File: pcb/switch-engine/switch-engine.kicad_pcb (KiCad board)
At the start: 10 copper layers, 135 x 111 mm, 369 parts, among them J1 CONN_PCIE_PWR_8PIN, J10 CORTEX_DEBUG_ETM, J11 SMPM, J12 CONN_01X03, J13 PMOD_HOST, J14 ARF6-08-S-D-A-K-TR, J15 ARF6-08-S-D-A-K-TR, J16 CONN_01X10, J17 ARF6-08-S-D-A-K-TR, J18 ARF6-08-S-D-A-K-TR, J19 CONN_01X10, J2 CONN_IBC_MGMT, J20 0826-1G1T-23-F, J21 ARF6-08-S-D-A-K-TR, J22 ARF6-08-S-D-A-K-TR, J23 CONN_01X10, J24 SMPM, J26 RJ45, J3 CONN_01X03, J4 CORTEX_DEBUG_ETM, J5 FAN_01, J6 FAN_01, J7 JUMPER_0402, J8 XILINX_JTAG, J9 PMOD_HOST, M1 SCREWHOLE, M2 SCREWHOLE, M3 SCREWHOLE, M4 SCREWHOLE, M5 LOGO, M6 LOGO, M7 LOGO, M8 960-27-23-D-AB-0, M9 FAN, Q2 SSM6N58NU, SW1 SWITCH, SW2 SWITCH, U1 STM32L431-QFN48, U10 74LVC1T45, U11 74LVC1T45, U12 74LVC1T45, U13 MT25QU256ABA8E12-0AUT, U14 ECS-1612MV-250-CN, U15 SIT9121AI-2BF-XXS156.250000G, U17 AT24MAC402, U18 74LVC1T45, U19 74LVC1T45, U2 MYMGK1R812ERSR, U20 74LVC1T45, U21 74LVC1T45, U22 ECS-1612MV-250-CN, U23 KSZ9031RN, U24 ESD224DQAR, U25 SIT9121AI-2BF-XXS156.250000G, U26 ESD224DQAR, U27 SIT9121AI-2BF-XXS156.250000G, U28 ADP1740ACPZ-2.5-R7, U29 ADM3101E_QFN, U3 MYMGK1R812ERSR, U4 MYMGK00506ERSR, U5 MYMGK00504ERSR, U6 MYMGK00504ERSR, U7 ADP1740ACPZ-1.8-R7, U8 XCKU5P-2FFVB676I, U9 STM32H735-UFBGA176-25

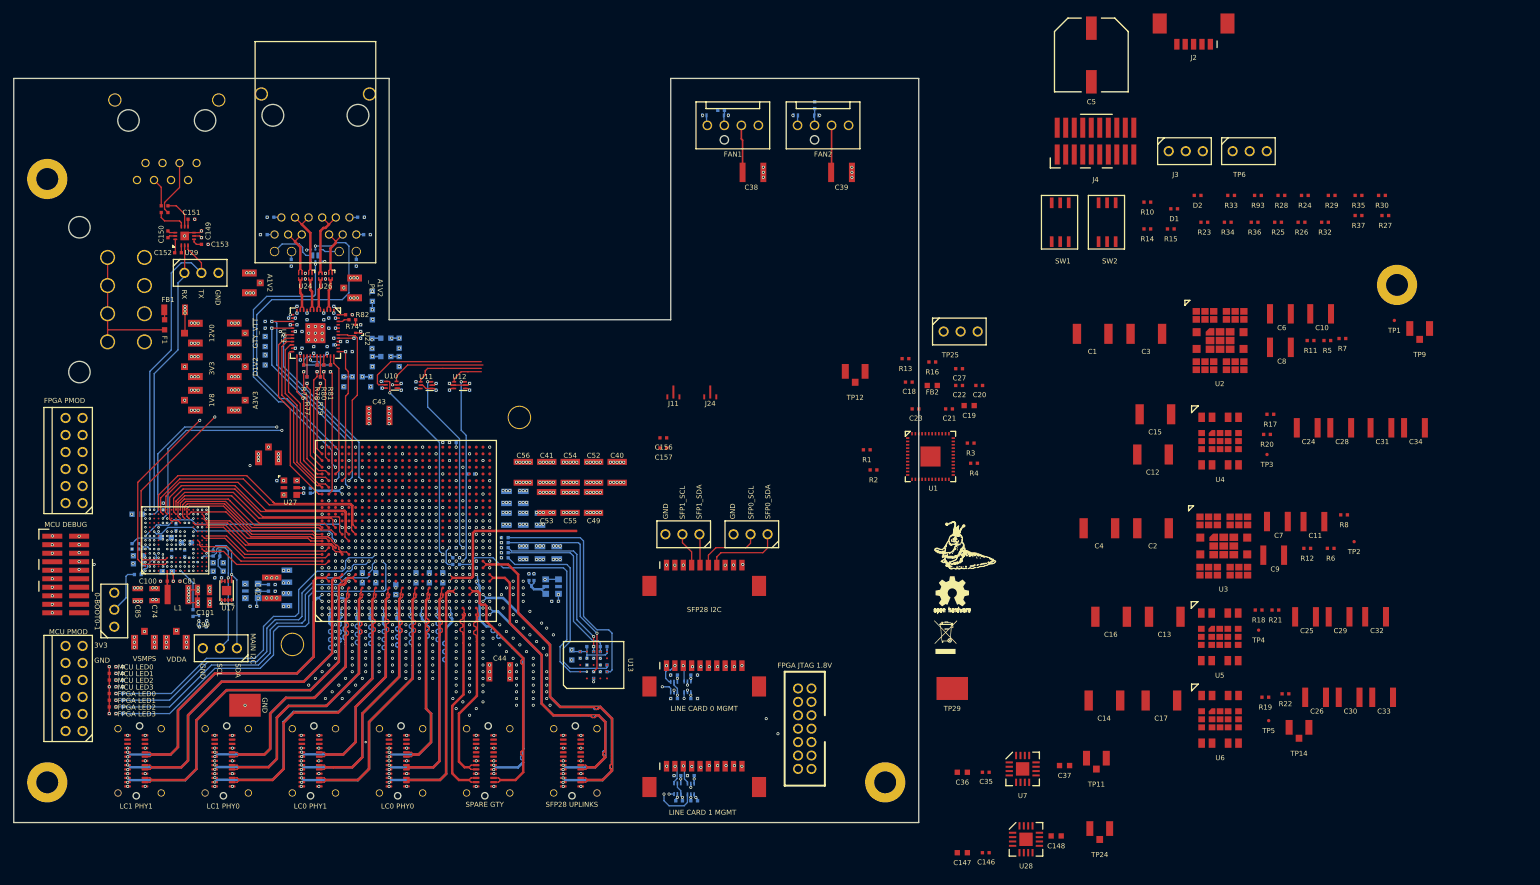
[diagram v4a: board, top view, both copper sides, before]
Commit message: Started routing supervisor area in northeast corner
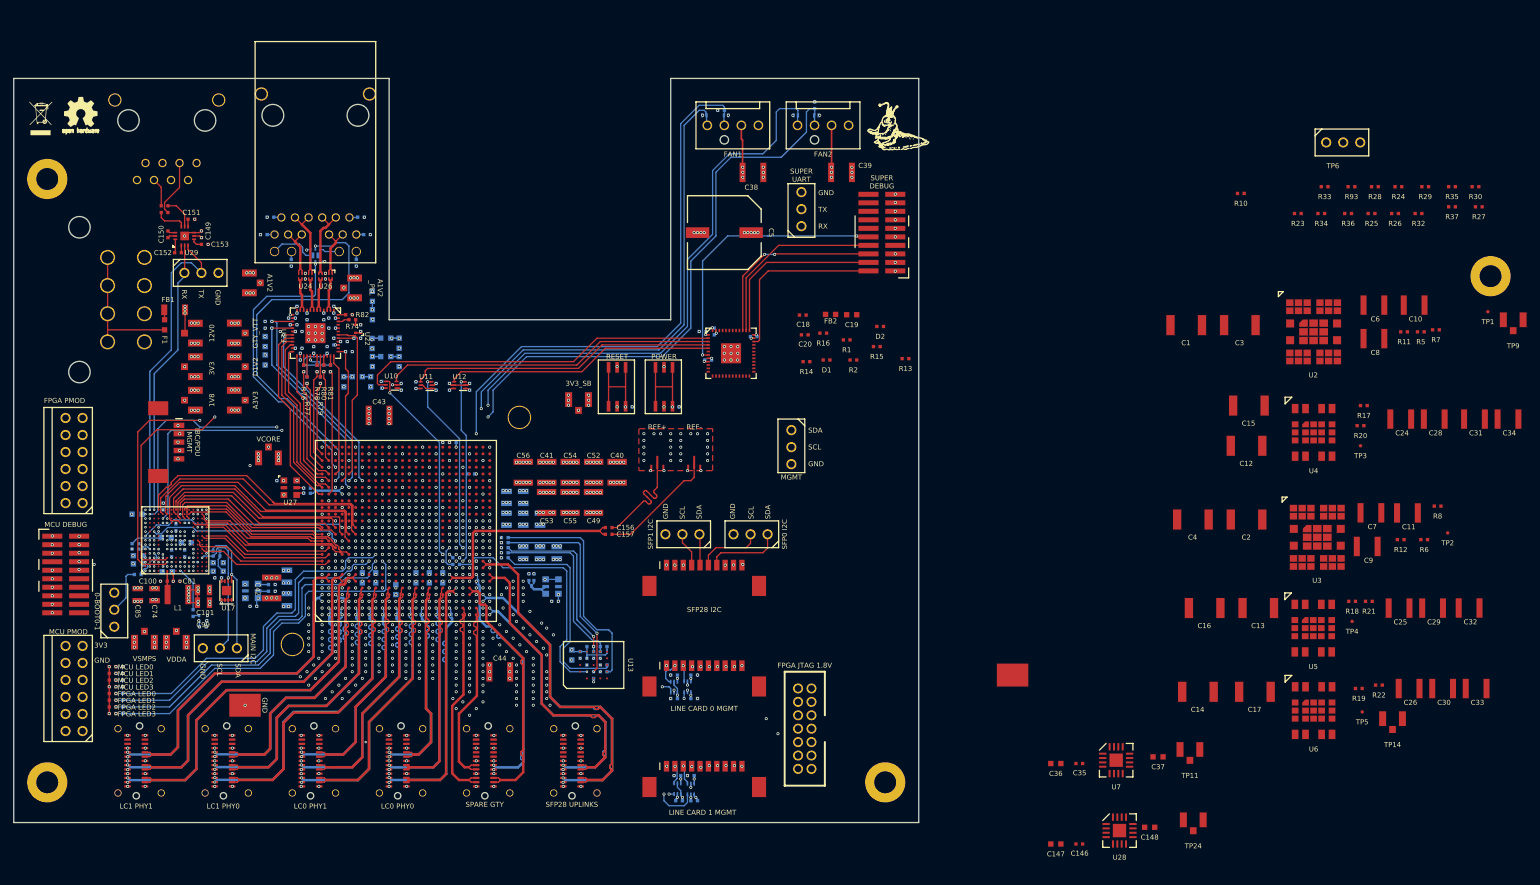
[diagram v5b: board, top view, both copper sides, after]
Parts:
- C21, C22, C23, C27, R3, R4: moved to B.Cu
- moved J2 162.6 mm to (61.6, 85.2), turned to 90 degrees
- moved M7 155.6 mm to (41.0, 37.0)
- moved M6 148.4 mm to (47.0, 36.0)
- moved SW1 70.5 mm to (127.0, 77.0)
- moved SW2 70.5 mm to (134.0, 77.0)
- moved M5 63.3 mm to (169.5, 38.5)
- moved C5 60.8 mm to (143.0, 54.0), turned to -90 degrees
- moved J3 58.0 mm to (154.5, 50.5), turned to 90 degrees
- moved D1 56.5 mm to (158.2, 73.0)
- moved R14 54.6 mm to (155.2, 73.2)
- moved R3 51.3 mm to (128.8, 80.0), turned to 180 degrees
- moved D2 51.2 mm to (166.2, 68.0)
- moved R15 47.2 mm to (165.8, 71.0)
- moved R4 45.3 mm to (135.8, 80.0), turned to 180 degrees
- moved TP12 41.5 mm to (121.2, 79.0)
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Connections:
- U1 pad 14: /FPGA support/FPGA_DONE_3V3 -> /Power Supply/1V8_EN
- U1 pad 2: /Power Supply/VCCINT_EN -> /FPGA support/FPGA_INIT_OE
- U1 pad 20: /FPGA support/FPGA_INIT_3V3 -> /Power Supply/1V8_PGOOD
- U1 pad 25: /FPGA support/FPGA_RESET_N_3V3 -> /Power Supply/SUPER_LED0
- U1 pad 28: /FPGA support/FPGA_INIT_OE -> /Power Supply/VCCINT_EN
- U1 pad 3: /Power Supply/1V8_PGOOD -> /FPGA support/FPGA_INIT_3V3
- U1 pad 4: /Power Supply/1V8_EN -> /FPGA support/FPGA_DONE_3V3
- U1 pad 5: /Power Supply/SUPER_LED0 -> /FPGA support/FPGA_RESET_N_3V3
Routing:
- net /GND: track 1760.9 -> 1918.2 mm, vias 748 -> 826
- net /MCU/3V3_SB: track 185.3 -> 324.4 mm, vias 1 -> 13
- net /Power Supply/FAN2_TACH: track 48.3 -> 140.2 mm, vias 1 -> 2
- net /Power Supply/FAN2_PWM: track 53.7 -> 142.4 mm, vias 1 -> 2
- net /Power Supply/FAN1_TACH: track 44.8 -> 131.1 mm, vias 1 -> 2
- net /Power Supply/FAN1_PWM: track 52.7 -> 132.5 mm, vias 1 -> 2
- net /Power Supply/SUPER_I2C_SDA: track 0.00 -> 75.8 mm, vias 0 -> 1
- net /Power Supply/SUPER_I2C_SCL: track 0.00 -> 73.6 mm, vias 0 -> 1
- net /Power Supply/12V0_EN: track 0.00 -> 68.4 mm, vias 0 -> 1
- net /MCU/SFP0_SCL: track 58.1 -> 123.7 mm
- net /MCU/SFP0_SDA: track 54.9 -> 114.1 mm
- net /Power Supply/12V0: track 103.6 -> 155.1 mm, vias 3 -> 14
- net /MCU/SFP1_SDA: track 63.7 -> 108.6 mm
- net /MCU/SFP1_SCL: track 65.0 -> 106.5 mm
- net /Power Supply/SUPER_RST_N: track 0.00 -> 41.2 mm, vias 0 -> 2
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- added copper zone on F.Cu, net /GND
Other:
- board text added: "3V3_SB"
- board text added: "IBC/PDU MGMT"
- board text added: "MGMT"
- board text added: "POWER"
- board text added: "REF+"
- board text added: "REF-"
- board text added: "RESET"
- board text added: "SFP0 I2C"
- board text added: "SFP1 I2C"
- board text added: "SUPER DEBUG"
- board text added: "SUPER UART"
- board text added: "VCORE"
- board text removed: "SFP0_SCL"
- board text removed: "SFP0_SDA"
- board text removed: "SFP1_SCL"
- board text removed: "SFP1_SDA"

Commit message: More work on supervisor area
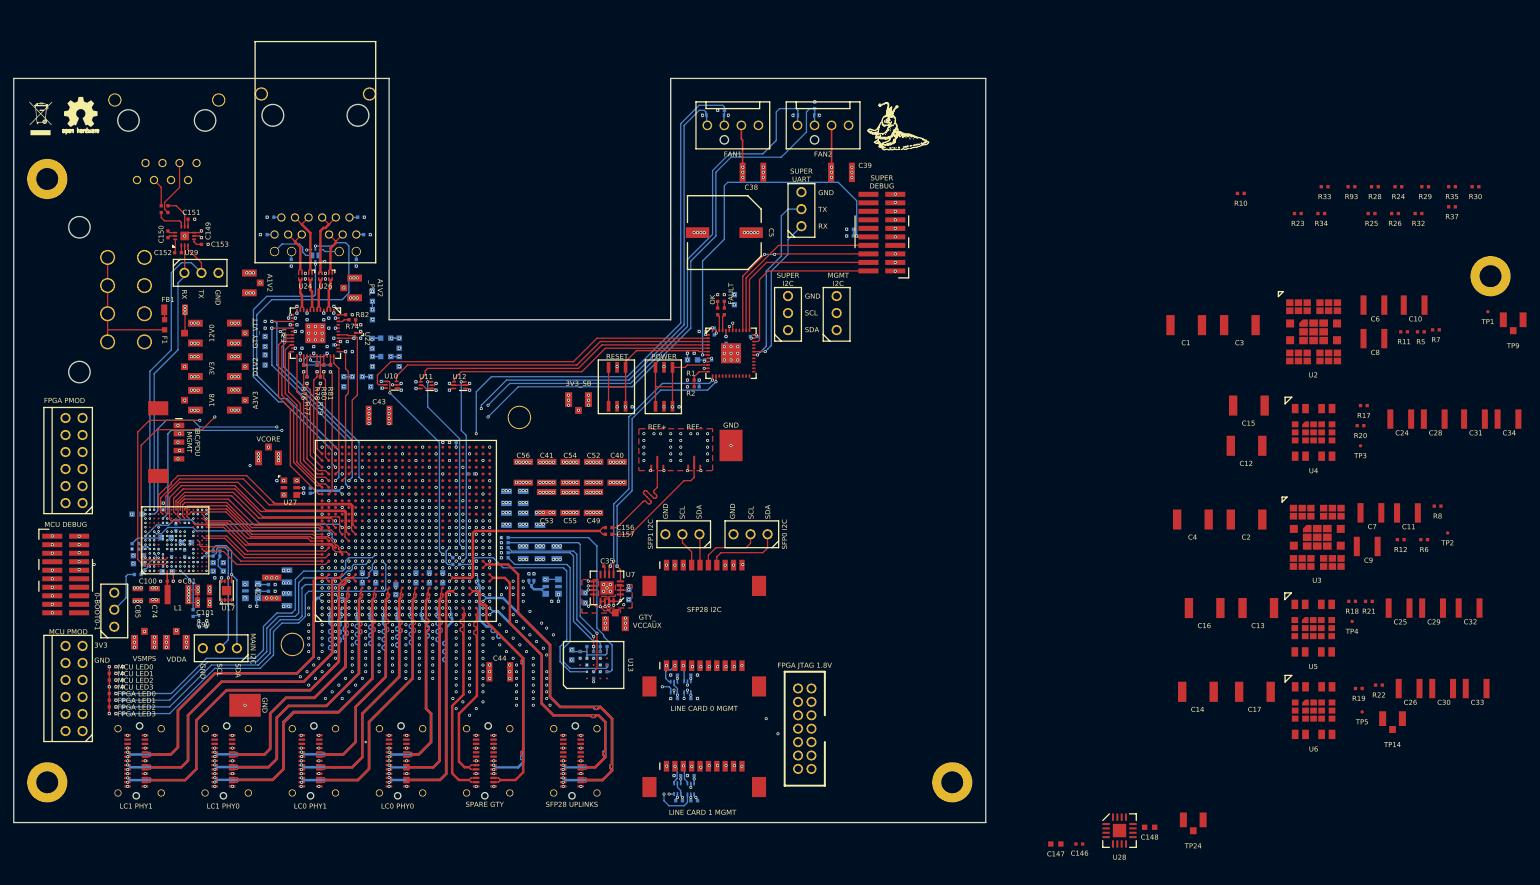
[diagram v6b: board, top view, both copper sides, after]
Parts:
- C18, C19, C20, C36, C37, FB2, R13, R16, R27, R36: moved to B.Cu
- moved R27 139.7 mm to (126.5, 103.8), turned to 180 degrees
- moved R36 100.1 mm to (139.2, 76.5), turned to 90 degrees
- moved C37 88.7 mm to (122.2, 108.5), turned to -90 degrees
- moved TP11 87.8 mm to (126.8, 112.2), turned to 180 degrees
- moved TP6 86.6 mm to (152.5, 66.0), turned to 90 degrees
- moved U7 80.2 mm to (125.5, 107.0), turned to 180 degrees
- moved C35 76.4 mm to (125.5, 103.8)
- moved C36 68.5 mm to (128.8, 108.0), turned to -90 degrees
- moved TP29 54.2 mm to (144.0, 85.8), turned to 90 degrees
- moved R13 26.9 mm to (143.2, 70.0), turned to -90 degrees
- moved R2 24.6 mm to (138.0, 77.0), turned to 180 degrees
- moved R1 24.0 mm to (138.0, 76.0)
- moved D2 23.6 mm to (143.0, 63.8), turned to -90 degrees
- moved R15 23.3 mm to (143.0, 65.8), turned to -90 degrees
- moved FB2 21.7 mm to (138.2, 73.0), turned to 180 degrees
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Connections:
- U1 pad 10: /Power Supply/3V3_EN -> /Power Supply/SOFT_POWER
- U1 pad 11: /Power Supply/3V3_PGOOD -> /MCU/MCU_RST_N
- U1 pad 12: /Power Supply/12V0_EN -> /Power Supply/12V0_VMON
- U1 pad 13: /Power Supply/GTY_VCC_EN -> /Power Supply/GTY_VCCAUX_PGOOD
- U1 pad 14: /Power Supply/1V8_EN -> /Power Supply/GTY_VCCAUX_EN
- U1 pad 16: /Power Supply/GTY_VCCAUX_PGOOD -> /Power Supply/GTY_VCC_EN
- U1 pad 19: /Power Supply/12V0_VMON -> /Power Supply/12V0_EN
- U1 pad 25: /Power Supply/SUPER_LED0 -> /Power Supply/2V5_PGOOD
- U1 pad 32: /Power Supply/GTY_VCCAUX_EN -> /Power Supply/1V8_EN
- U1 pad 33: /Power Supply/SOFT_POWER -> /Power Supply/3V3_PGOOD
- U1 pad 41: /Power Supply/SOFT_RESET -> /Power Supply/3V3_EN
- U1 pad 45: /Power Supply/2V5_PGOOD -> /Power Supply/SUPER_LED1
- U1 pad 46: /MCU/MCU_RST_N -> /Power Supply/SUPER_LED0
- U1 pad 6: /Power Supply/SUPER_LED1 -> /Power Supply/SOFT_RESET
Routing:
- net /GND: track 1918.2 -> 2009.2 mm, vias 826 -> 847
- net /Power Supply/GTY_VCCAUX_EN: track 0.00 -> 41.0 mm, vias 0 -> 2
- net /Power Supply/GTY_VCCAUX_PGOOD: track 0.00 -> 40.3 mm, vias 0 -> 2
- net /Power Supply/SUPER_I2C_SDA: track 75.8 -> 113.0 mm, vias 1 -> 2
- net /Power Supply/SUPER_I2C_SCL: track 73.6 -> 106.0 mm, vias 1 -> 2
- net /MCU/3V3_SB: track 324.4 -> 351.8 mm, vias 13 -> 18
- net /Power Supply/SUPER_UART_TX: track 0.00 -> 26.2 mm, vias 0 -> 1
- net /Power Supply/SUPER_UART_RX: track 0.00 -> 22.6 mm, vias 0 -> 1
- net /FPGA support/GTY_VCCAUX: track 22.6 -> 40.8 mm, vias 2 -> 9
- net /Power Supply/SUPER_RST_N: track 41.2 -> 57.1 mm
- net /3V3: track 516.0 -> 531.8 mm, vias 72 -> 78
- net /Power Supply/SOFT_RESET: track 14.2 -> 28.2 mm
- net /Power Supply/12V0: track 155.1 -> 163.4 mm, vias 14 -> 15
- net /Power Supply/SOFT_POWER: track 14.2 -> 19.7 mm
- net /Line card interfaces/LC0_SPI_CS_N: track 49.1 -> 53.5 mm
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- added copper zone on F.Cu, net /3V3
- added copper zone on F.Cu, net /FPGA support/GTY_VCCAUX
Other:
- board size 135 x 111 mm -> 145 x 111 mm
- board text added: "FAULT"
- board text added: "GTY_ VCCAUX"
- board text added: "MGMT I2C"
- board text added: "OK"
- board text added: "SUPER I2C"
- board text removed: "MGMT"
